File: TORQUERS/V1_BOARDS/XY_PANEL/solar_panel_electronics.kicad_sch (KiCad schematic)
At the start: 32 parts, among them U3 LTC3130EUDC-1-PBF

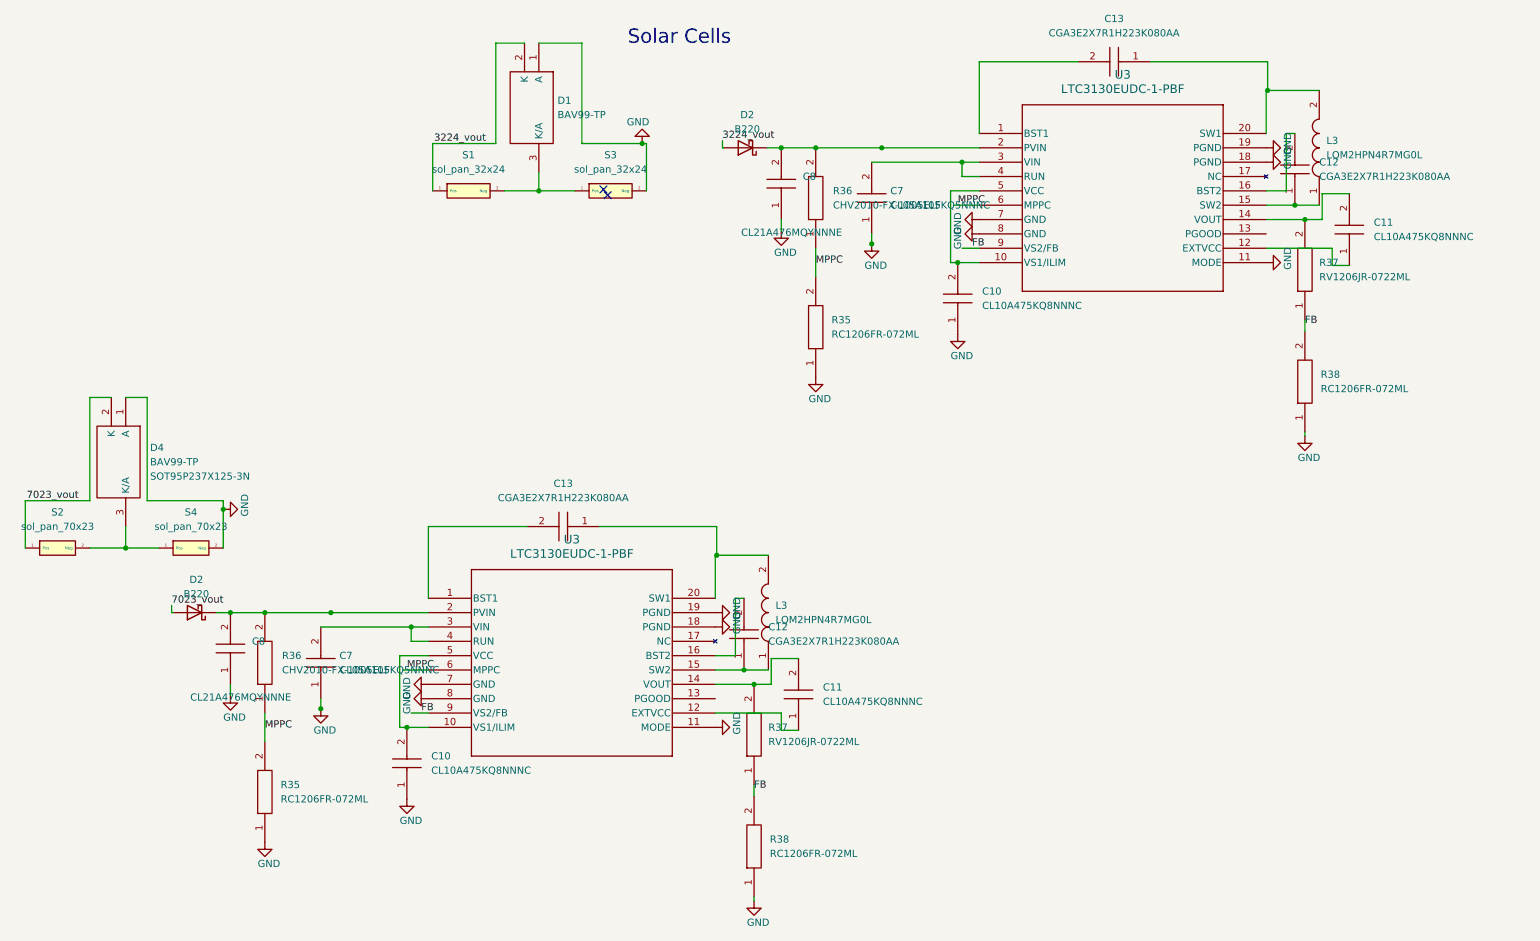
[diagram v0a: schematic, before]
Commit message: Schematic lock on XY BOARD
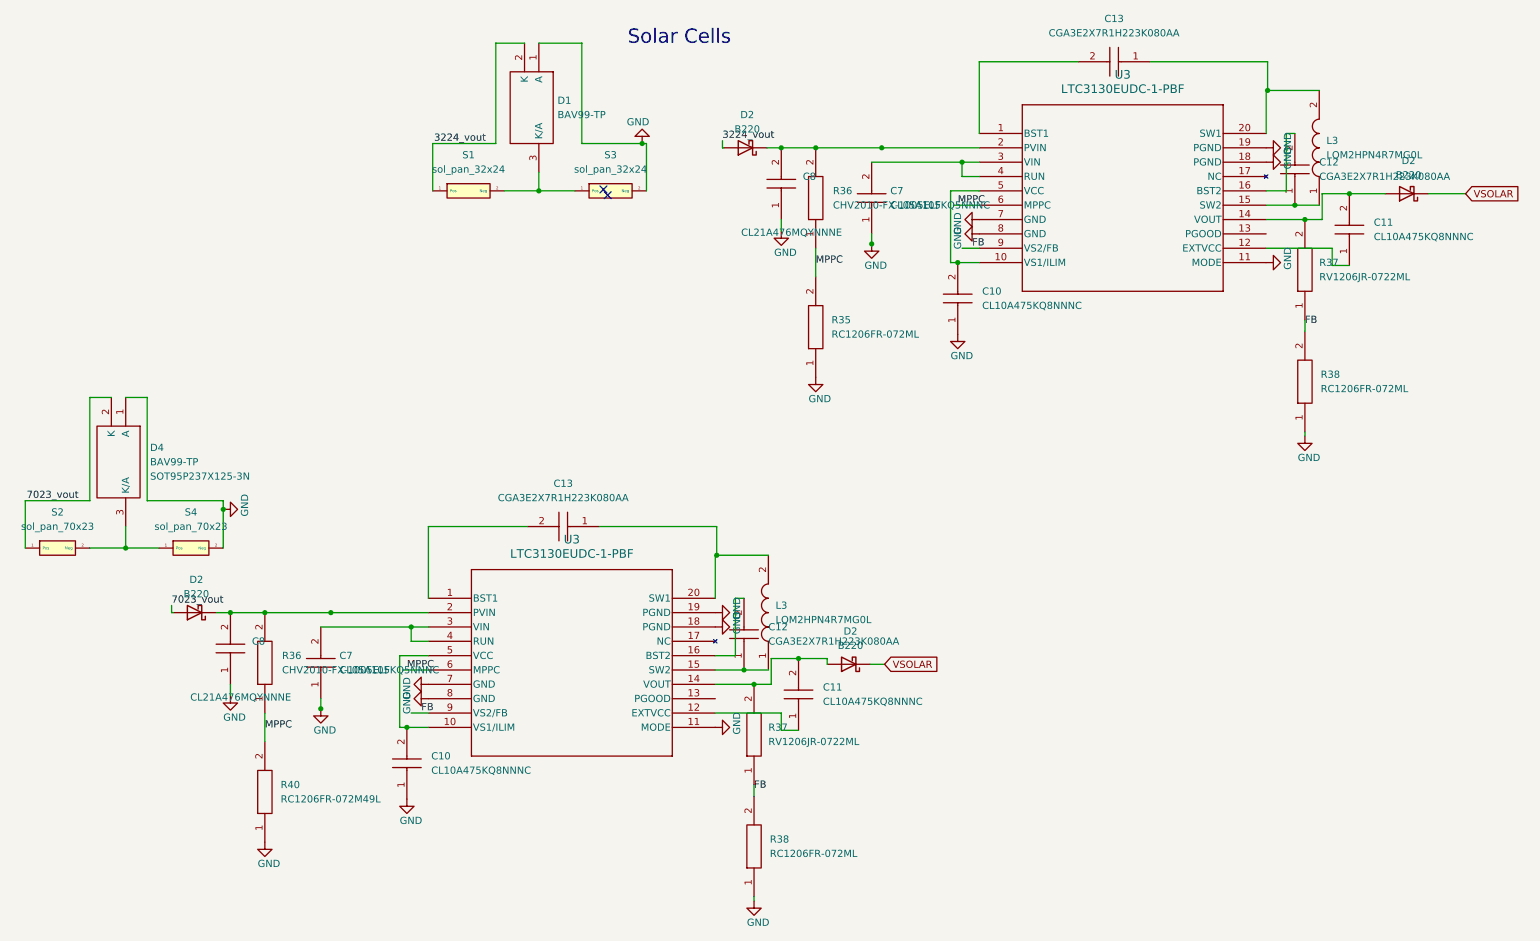
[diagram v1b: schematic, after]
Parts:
- removed R35: RC1206FR-072ML, RESC3116X65N, symbol AA_AUTO_LOADER:RC1206FR-072ML
- added D2 (x2): B220, Diode_SMD:D_SMB, symbol Diode:B220
- added R40: RC1206FR-072M49L, RESC3116X65N, symbol AA_AUTO_LOADER:RC1206FR-072M49L
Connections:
- net GND: now also R40.1
- net MPPC: now also R40.2
- net at C11.2, R37.2, U3.14 (VOUT): now also D2.2 (A) (x2)
- new net VSOLAR: D2.1 (K), D2.1 (K)
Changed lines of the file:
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@@
   (junction (at 148.336 43.18) (diameter 0) (color 0 0 0 0)
   )
+  (junction (at 151.384 133.604) (diameter 0) (color 0 0 0 0)
+  )
   (junction (at 49.53 107.188) (diameter 0) (color 0 0 0 0)
   )
@@
   )
   (junction (at 50.8 125.476) (diameter 0) (color 0 0 0 0)
+  )
+  (junction (at 248.92 51.308) (diameter 0) (color 0 0 0 0)
   )
   (junction (at 68.58 125.476) (diameter 0) (color 0 0 0 0)
@@
     (stroke (width 0) (type default))
   )
+  (wire (pts (xy 156.464 133.604) (xy 151.384 133.604))
+    (stroke (width 0) (type default))
+  )
   (wire (pts (xy 124.46 42.418) (xy 124.46 50.8))
     (stroke (width 0) (type default))
@@
     (stroke (width 0) (type default))
   )
+  (wire (pts (xy 262.89 51.308) (xy 269.494 51.308))
+    (stroke (width 0) (type default))
+  )
   (wire (pts (xy 213.614 27.94) (xy 234.442 27.94))
     (stroke (width 0) (type default))
@@
     (stroke (width 0) (type default))
   )
+  (wire (pts (xy 164.084 134.62) (xy 166.624 134.62))
+    (stroke (width 0) (type default))
+  )
   (wire (pts (xy 99.314 50.8) (xy 105.41 50.8))
     (stroke (width 0) (type default))
@@
     (stroke (width 0) (type default))
   )
+  (wire (pts (xy 255.27 51.308) (xy 248.92 51.308))
+    (stroke (width 0) (type default))
+  )
   (wire (pts (xy 123.698 42.418) (xy 124.46 42.418))
     (stroke (width 0) (type default))
@@
   )
   (wire (pts (xy 80.772 145.796) (xy 82.042 145.796))
+    (stroke (width 0) (type default))
+  )
+  (wire (pts (xy 156.464 134.62) (xy 156.464 133.604))
     (stroke (width 0) (type default))
   )
@@
   (label "FB" (at 143.51 156.972 0) (fields_autoplaced)
     (effects (font (size 1.27 1.27)) (justify left bottom))
+  )
+  (global_label "VSOLAR" (shape input) (at 269.494 51.308 0) (fields_autoplaced)
+    (effects (font (size 1.27 1.27)) (justify left))
+    (property "Intersheetrefs" "${INTERSHEET_REFS}" (at 279.4945 51.308 0)
+      (effects (font (size 1.27 1.27)) (justify left) hide)
+    )
+  )
+  (global_label "VSOLAR" (shape input) (at 166.624 134.62 0) (fields_autoplaced)
+    (effects (font (size 1.27 1.27)) (justify left))
+    (property "Intersheetrefs" "${INTERSHEET_REFS}" (at 176.6245 134.62 0)
+      (effects (font (size 1.27 1.27)) (justify left) hide)
+    )
   )
   (symbol (lib_id "power:GND") (at 136.652 145.796 90) (mirror x) (unit 1)
@@
         (path "/97119169-578f-44be-8822-faf8f0e4fcd6/db306d3f-1ab7-4e38-afab-c78bdb56c587"
           (reference "#PWR010") (unit 1)
+        )
+      )
+    )
+  )
+  (symbol (lib_id "AA_AUTO_LOADER:RC1206FR-072M49L") (at 56.896 166.116 90) (unit 1)
+    (in_bom yes) (on_board yes) (dnp no) (fields_autoplaced)
+    (property "Reference" "R40" (at 59.69 155.956 90)
+      (effects (font (size 1.27 1.27)) (justify right))
+    )
+    (property "Value" "RC1206FR-072M49L" (at 59.69 158.496 90)
+      (effects (font (size 1.27 1.27)) (justify right))
+    )
+    (property "Footprint" "RESC3116X65N" (at 55.626 152.146 0)
+      (effects (font (size 1.27 1.27)) (justify left) hide)
+    )
+    (property "Datasheet" "https://www.sos.sk/productdata/35/10/4/35104/RC1206.pdf" (at 58.166 152.146 0)
+      (effects (font (size 1.27 1.27)) (justify left) hide)
+    )
+    (property "Description" "Thick Film Resistors - SMD 1/4W 2.49M Ohms 1%" (at 60.706 152.146 0)
+      (effects (font (size 1.27 1.27)) (justify left) hide)
+    )
+    (property "Height" "0.65" (at 63.246 152.146 0)
+      (effects (font (size 1.27 1.27)) (justify left) hide)
+    )
+    (property "Manufacturer_Name" "KEMET" (at 65.786 152.146 0)
+      (effects (font (size 1.27 1.27)) (justify left) hide)
+    )
+    (property "Manufacturer_Part_Number" "RC1206FR-072M49L" (at 68.326 152.146 0)
+      (effects (font (size 1.27 1.27)) (justify left) hide)
+    )
+    (property "Mouser Part Number" "603-RC1206FR-072M49L" (at 70.866 152.146 0)
+      (effects (font (size 1.27 1.27)) (justify left) hide)
+    )
+    (property "Mouser Price/Stock" "https://www.mouser.com/Search/Refine.aspx?Keyword=603-RC1206FR-072M49L" (at 73.406 152.146 0)
+      (effects (font (size 1.27 1.27)) (justify left) hide)
+    )
+    (property "Arrow Part Number" "RC1206FR-072M49L" (at 75.946 152.146 0)
+      (effects (font (size 1.27 1.27)) (justify left) hide)
+    )
+    (property "Arrow Price/Stock" "https://www.arrow.com/en/products/rc1206fr-072m49l/yageo" (at 78.486 152.146 0)
+      (effects (font (size 1.27 1.27)) (justify left) hide)
+    )
+    (pin "1")
+    (pin "2")
+    (instances
+      (project "Xpanel_V1_final"
+        (path "/97119169-578f-44be-8822-faf8f0e4fcd6/db306d3f-1ab7-4e38-afab-c78bdb56c587"
+          (reference "R40") (unit 1)
         )
       )
@@
     )
   )
+  (symbol (lib_id "Diode:B220") (at 160.274 134.62 180) (unit 1)
+    (in_bom yes) (on_board yes) (dnp no) (fields_autoplaced)
+    (property "Reference" "D2" (at 160.5915 128.778 0)
+      (effects (font (size 1.27 1.27)))
+    )
+    (property "Value" "B220" (at 160.5915 131.318 0)
+      (effects (font (size 1.27 1.27)))
+    )
+    (property "Footprint" "Diode_SMD:D_SMB" (at 160.274 130.175 0)
+      (effects (font (size 1.27 1.27)) hide)
+    )
+    (property "Datasheet" "http://www.jameco.com/Jameco/Products/ProdDS/1538777.pdf" (at 160.274 134.62 0)
+      (effects (font (size 1.27 1.27)) hide)
+    )
+    (pin "1")
+    (pin "2")
+    (instances
+      (project "Xpanel_V1_final"
+        (path "/97119169-578f-44be-8822-faf8f0e4fcd6"
+          (reference "D2") (unit 1)
+        )
+        (path "/97119169-578f-44be-8822-faf8f0e4fcd6/db306d3f-1ab7-4e38-afab-c78bdb56c587"
+          (reference "D7") (unit 1)
+        )
+      )
+    )
+  )
   (symbol (lib_id "AA_AUTO_LOADER:RC1206FR-072ML") (at 143.51 175.768 90) (unit 1)
     (in_bom yes) (on_board yes) (dnp no) (fields_autoplaced)
@@
     )
   )
-  (symbol (lib_id "AA_AUTO_LOADER:RC1206FR-072ML") (at 56.896 166.116 90) (unit 1)
-    (in_bom yes) (on_board yes) (dnp no) (fields_autoplaced)
-    (property "Reference" "R35" (at 59.69 155.956 90)
-      (effects (font (size 1.27 1.27)) (justify right))
-    )
-    (property "Value" "RC1206FR-072ML" (at 59.69 158.496 90)
-      (effects (font (size 1.27 1.27)) (justify right))
-    )
-    (property "Footprint" "RESC3116X65N" (at 55.626 152.146 0)
-      (effects (font (size 1.27 1.27)) (justify left) hide)
-    )
-    (property "Datasheet" "https://www.sos.sk/productdata/35/10/4/35104/RC1206.pdf" (at 58.166 152.146 0)
-      (effects (font (size 1.27 1.27)) (justify left) hide)
-    )
-    (property "Description" "Yageo RC1206 Series Thick Film Surface Mount Resistor 1206 Case 2M +/-1% 0.25W +/-100ppm/C" (at 60.706 152.146 0)
-      (effects (font (size 1.27 1.27)) (justify left) hide)
-    )
-    (property "Height" "0.65" (at 63.246 152.146 0)
-      (effects (font (size 1.27 1.27)) (justify left) hide)
-    )
-    (property "Manufacturer_Name" "KEMET" (at 65.786 152.146 0)
-      (effects (font (size 1.27 1.27)) (justify left) hide)
-    )
-    (property "Manufacturer_Part_Number" "RC1206FR-072ML" (at 68.326 152.146 0)
-      (effects (font (size 1.27 1.27)) (justify left) hide)
-    )
-    (property "Mouser Part Number" "603-RC1206FR-072ML" (at 70.866 152.146 0)
-      (effects (font (size 1.27 1.27)) (justify left) hide)
-    )
-    (property "Mouser Price/Stock" "https://www.mouser.co.uk/ProductDetail/Yageo/RC1206FR-072ML?qs=fiyQ2z0a5elvbAYRlue2vA%3D%3D" (at 73.406 152.146 0)
-      (effects (font (size 1.27 1.27)) (justify left) hide)
-    )
-    (property "Arrow Part Number" "" (at 75.946 152.146 0)
-      (effects (font (size 1.27 1.27)) (justify left) hide)
-    )
-    (property "Arrow Price/Stock" "" (at 78.486 152.146 0)
-      (effects (font (size 1.27 1.27)) (justify left) hide)
-    )
-    (pin "1")
-    (pin "2")
-    (instances
-      (project "Xpanel_V1_final"
-        (path "/97119169-578f-44be-8822-faf8f0e4fcd6"
-          (reference "R35") (unit 1)
-        )
-        (path "/97119169-578f-44be-8822-faf8f0e4fcd6/db306d3f-1ab7-4e38-afab-c78bdb56c587"
-          (reference "R40") (unit 1)
-        )
-      )
-    )
-  )
   (symbol (lib_id "power:GND") (at 123.698 42.418 0) (mirror x) (unit 1)
     (in_bom yes) (on_board yes) (dnp no)
@@
         )
       )
+    )
+  )
+  (symbol (lib_id "Diode:B220") (at 259.08 51.308 180) (unit 1)
+    (in_bom yes) (on_board yes) (dnp no)
+    (property "Reference" "D2" (at 259.3975 45.466 0)
+      (effects (font (size 1.27 1.27)))
+    )
+    (property "Value" "B220" (at 259.3975 48.006 0)
+      (effects (font (size 1.27 1.27)))
+    )
+    (property "Footprint" "Diode_SMD:D_SMB" (at 259.08 46.863 0)
+      (effects (font (size 1.27 1.27)) hide)
+    )
+    (property "Datasheet" "http://www.jameco.com/Jameco/Products/ProdDS/1538777.pdf" (at 259.08 51.308 0)
+      (effects (font (size 1.27 1.27)) hide)
+    )
+    (pin "1")
+    (pin "2")
+    (instances
+      (project "Xpanel_V1_final"
+        (path "/97119169-578f-44be-8822-faf8f0e4fcd6"
+          (reference "D2") (unit 1)
+        )
+        (path "/97119169-578f-44be-8822-faf8f0e4fcd6/db306d3f-1ab7-4e38-afab-c78bdb56c587"
+          (reference "D8") (unit 1)
+        )
+      )

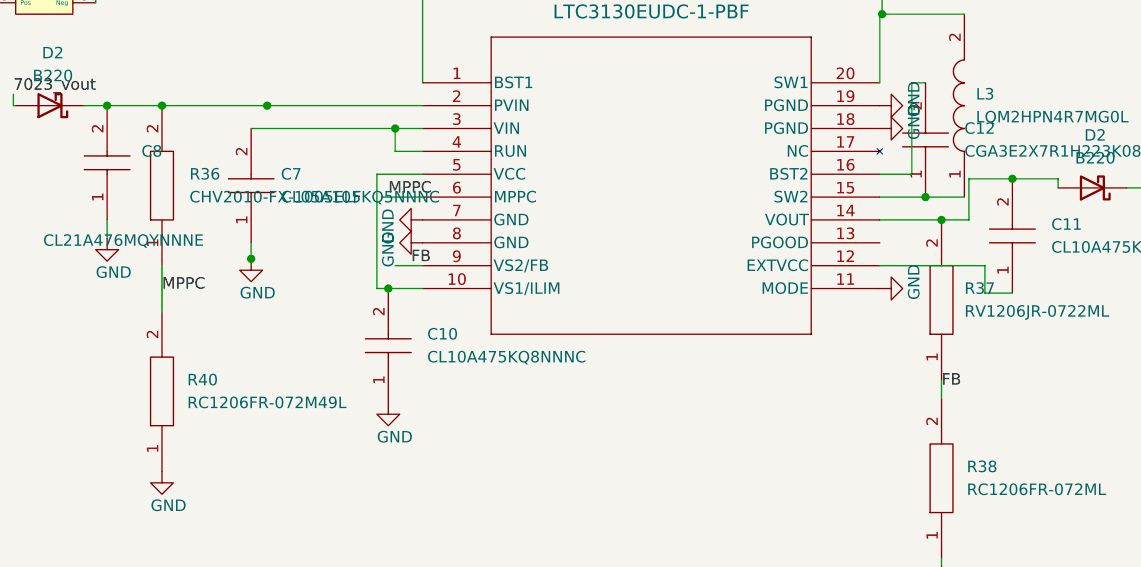
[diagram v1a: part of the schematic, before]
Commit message: completed XY Board
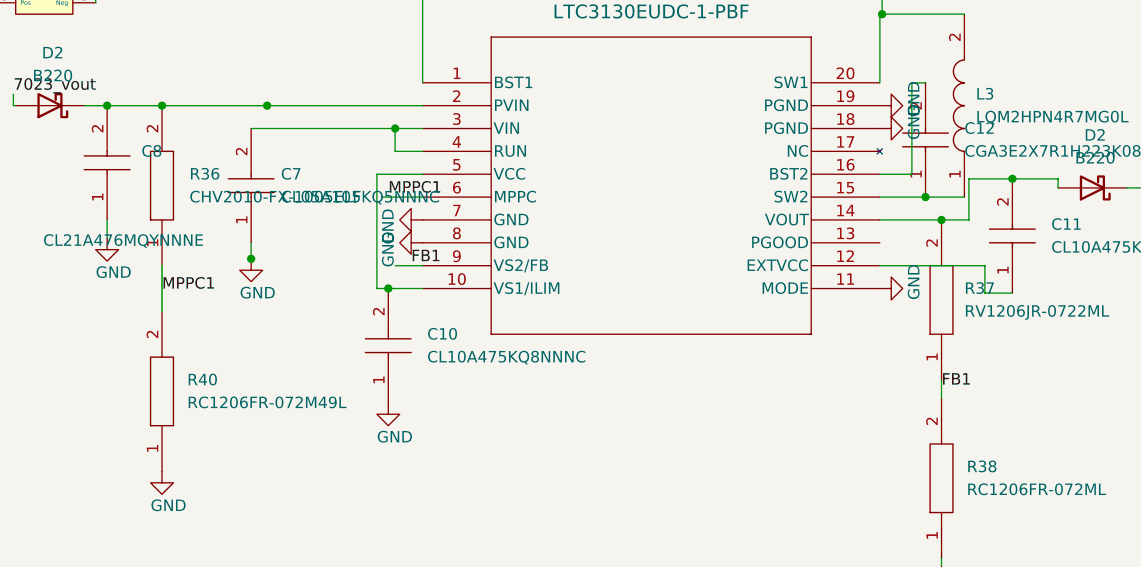
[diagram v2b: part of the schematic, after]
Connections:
- net FB: no longer R37.1, R38.2, U3.9 (VS2/FB)
- net MPPC: no longer R36.1, R40.2, U3.6 (MPPC)
- new net FB1: R37.1, R38.2, U3.9 (VS2/FB)
- new net MPPC1: R36.1, R40.2, U3.6 (MPPC)
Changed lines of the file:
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@@
     (effects (font (size 2.54 2.54)) (justify right bottom))
   )
-  (label "FB" (at 84.582 143.256 0) (fields_autoplaced)
+  (label "FB1" (at 84.582 143.256 0) (fields_autoplaced)
     (effects (font (size 1.27 1.27)) (justify left bottom))
   )
@@
     (effects (font (size 1.27 1.27)) (justify left bottom))
   )
-  (label "MPPC" (at 56.896 146.304 0) (fields_autoplaced)
+  (label "MPPC1" (at 56.896 146.304 0) (fields_autoplaced)
     (effects (font (size 1.27 1.27)) (justify left bottom))
   )
@@
     (effects (font (size 1.27 1.27)) (justify left bottom))
   )
-  (label "MPPC" (at 82.042 135.636 0) (fields_autoplaced)
+  (label "MPPC1" (at 82.042 135.636 0) (fields_autoplaced)
     (effects (font (size 1.27 1.27)) (justify left bottom))
   )
@@
     (effects (font (size 1.27 1.27)) (justify left bottom))
   )
-  (label "FB" (at 143.51 156.972 0) (fields_autoplaced)
+  (label "FB1" (at 143.51 156.972 0) (fields_autoplaced)
     (effects (font (size 1.27 1.27)) (justify left bottom))
   )
